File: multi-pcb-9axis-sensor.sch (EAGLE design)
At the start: 2 parts, among them X1 2.54B-ZR

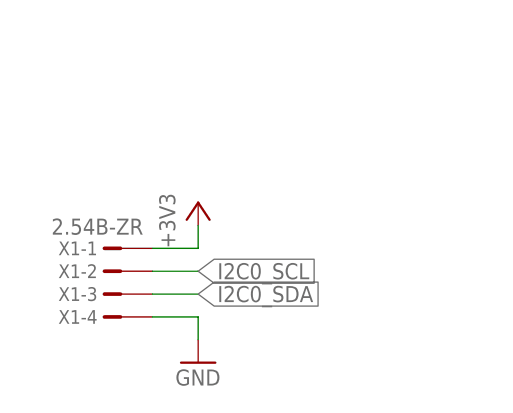
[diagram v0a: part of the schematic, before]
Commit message: Routed more multi-pcb boards
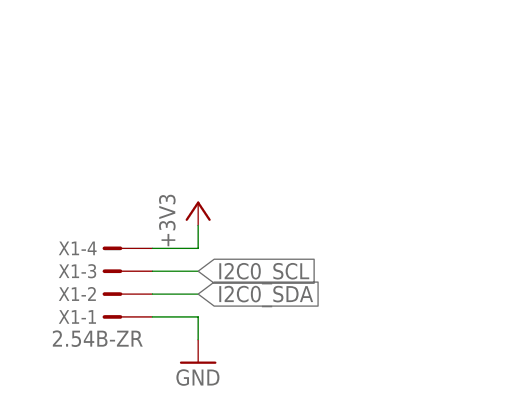
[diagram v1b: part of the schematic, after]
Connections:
- net +3V3: now also X1-4.1; no longer X1-1.1
- net GND: now also X1-1.1; no longer X1-4.1
- net I2C0_SCL: now also X1-3.1; no longer X1-2.1
- net I2C0_SDA: now also X1-2.1; no longer X1-3.1
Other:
- moved on the sheet: X1-1, X1-2, X1-3, X1-4
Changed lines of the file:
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@@
 <attribute name="VALUE" x="-109.22" y="-55.88" size="1.778" layer="96" rot="R90"/>
 </instance>
-<instance part="X1" gate="-1" x="-116.84" y="-55.88" smashed="yes" rot="MR0">
-<attribute name="NAME" x="-117.856" y="-56.642" size="1.524" layer="95" rot="MR0"/>
-<attribute name="VALUE" x="-112.776" y="-54.356" size="1.778" layer="96" rot="MR0"/>
+<instance part="X1" gate="-1" x="-116.84" y="-63.5" smashed="yes" rot="R180">
+<attribute name="NAME" x="-117.856" y="-62.738" size="1.524" layer="95" rot="R180"/>
+<attribute name="VALUE" x="-112.776" y="-65.024" size="1.778" layer="96" rot="R180"/>
 </instance>
-<instance part="X1" gate="-2" x="-116.84" y="-58.42" smashed="yes" rot="MR0">
-<attribute name="NAME" x="-117.856" y="-59.182" size="1.524" layer="95" rot="MR0"/>
+<instance part="X1" gate="-2" x="-116.84" y="-60.96" smashed="yes" rot="R180">
+<attribute name="NAME" x="-117.856" y="-60.198" size="1.524" layer="95" rot="R180"/>
 </instance>
-<instance part="X1" gate="-3" x="-116.84" y="-60.96" smashed="yes" rot="MR0">
-<attribute name="NAME" x="-117.856" y="-61.722" size="1.524" layer="95" rot="MR0"/>
+<instance part="X1" gate="-3" x="-116.84" y="-58.42" smashed="yes" rot="R180">
+<attribute name="NAME" x="-117.856" y="-57.658" size="1.524" layer="95" rot="R180"/>
 </instance>
-<instance part="X1" gate="-4" x="-116.84" y="-63.5" smashed="yes" rot="MR0">
-<attribute name="NAME" x="-117.856" y="-64.262" size="1.524" layer="95" rot="MR0"/>
+<instance part="X1" gate="-4" x="-116.84" y="-55.88" smashed="yes" rot="R180">
+<attribute name="NAME" x="-117.856" y="-55.118" size="1.524" layer="95" rot="R180"/>
 </instance>
 </instances>
@@
 <wire x1="-106.68" y1="-55.88" x2="-106.68" y2="-53.34" width="0.1524" layer="91"/>
 <pinref part="+3V1" gate="G$1" pin="+3V3"/>
-<pinref part="X1" gate="-1" pin="1"/>
-<wire x1="-106.68" y1="-55.88" x2="-111.76" y2="-55.88" width="0.1524" layer="91"/>
+<pinref part="X1" gate="-4" pin="1"/>
+<wire x1="-111.76" y1="-55.88" x2="-106.68" y2="-55.88" width="0.1524" layer="91"/>
 </segment>
 </net>
@@
 <wire x1="-106.68" y1="-63.5" x2="-106.68" y2="-66.04" width="0.1524" layer="91"/>
 <pinref part="GND15" gate="1" pin="GND"/>
-<pinref part="X1" gate="-4" pin="1"/>
+<pinref part="X1" gate="-1" pin="1"/>
 <wire x1="-106.68" y1="-63.5" x2="-111.76" y2="-63.5" width="0.1524" layer="91"/>
 </segment>
@@
 <segment>
 <label x="-106.68" y="-60.96" size="1.778" layer="95" xref="yes"/>
-<pinref part="X1" gate="-3" pin="1"/>
+<pinref part="X1" gate="-2" pin="1"/>
 <wire x1="-111.76" y1="-60.96" x2="-106.68" y2="-60.96" width="0.1524" layer="91"/>
 </segment>
@@
 <segment>
 <label x="-106.68" y="-58.42" size="1.778" layer="95" xref="yes"/>
-<pinref part="X1" gate="-2" pin="1"/>
+<pinref part="X1" gate="-3" pin="1"/>
 <wire x1="-106.68" y1="-58.42" x2="-111.76" y2="-58.42" width="0.1524" layer="91"/>
 </segment>

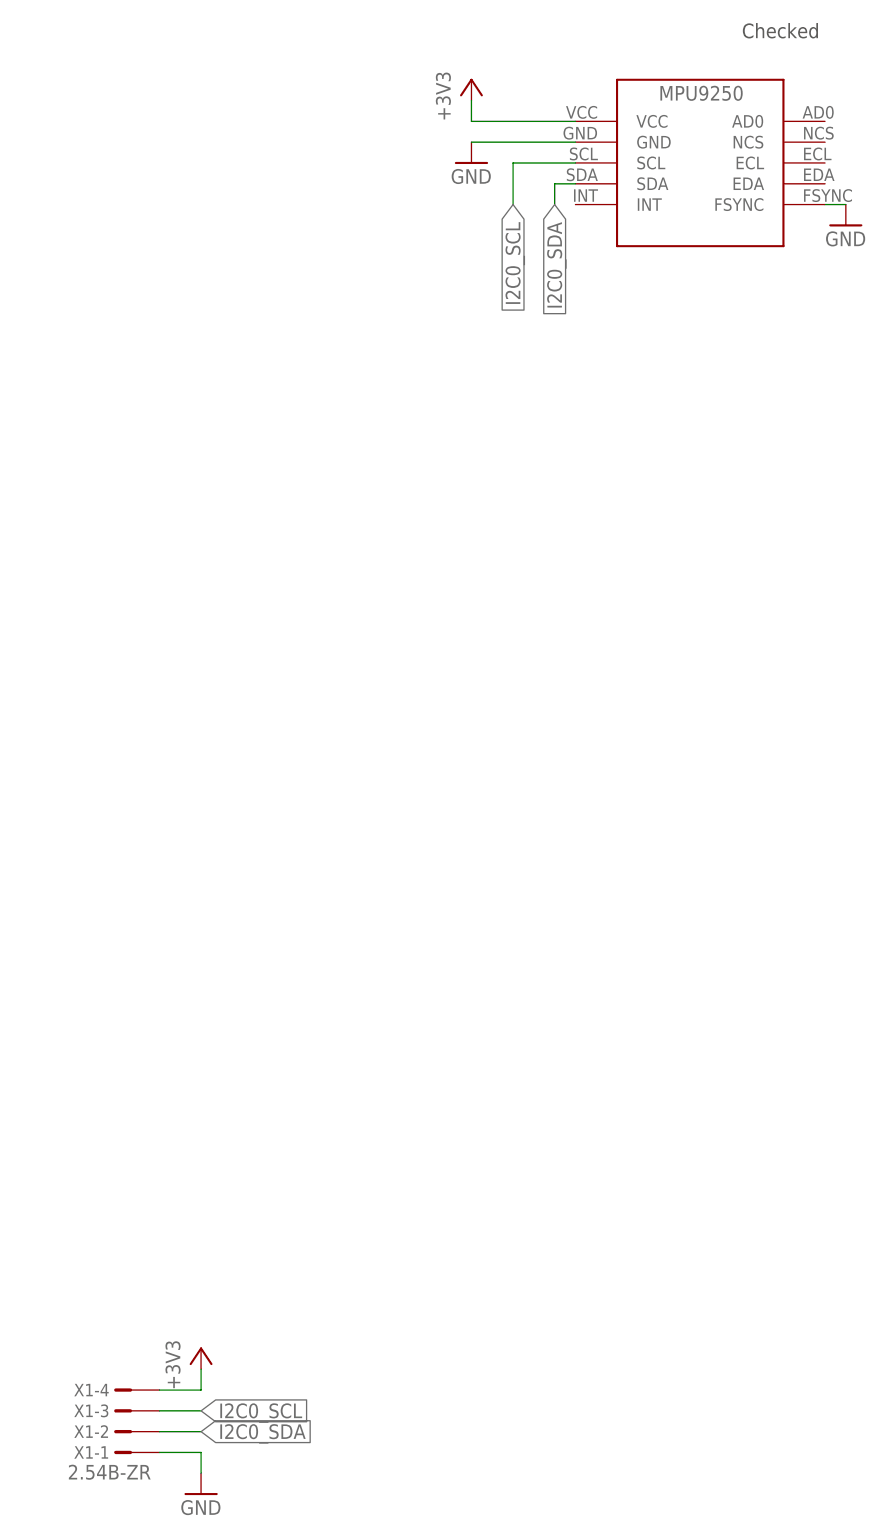
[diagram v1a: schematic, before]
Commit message: Made schematic more compact/clean
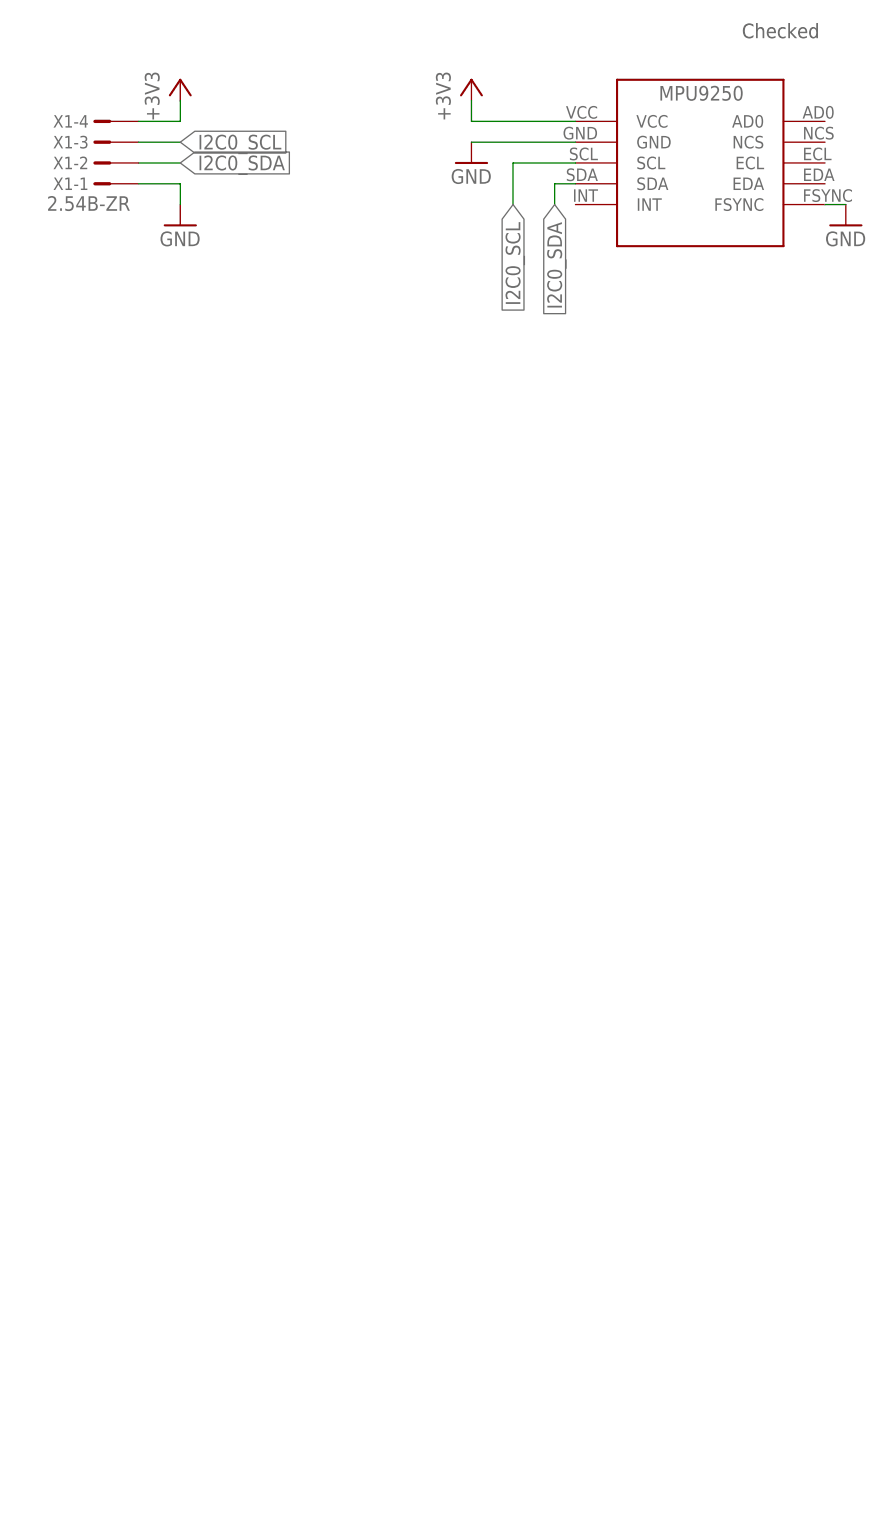
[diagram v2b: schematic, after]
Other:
- moved on the sheet: X1-1, X1-2, X1-3, X1-4
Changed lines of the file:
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@@
 <attribute name="VALUE" x="-30.48" y="83.82" size="1.778" layer="96"/>
 </instance>
-<instance part="GND15" gate="1" x="-106.68" y="-68.58" smashed="yes">
-<attribute name="VALUE" x="-109.22" y="-71.12" size="1.778" layer="96"/>
+<instance part="GND15" gate="1" x="-109.22" y="86.36" smashed="yes">
+<attribute name="VALUE" x="-111.76" y="83.82" size="1.778" layer="96"/>
 </instance>
 <instance part="+3V5" gate="G$1" x="-73.66" y="104.14" smashed="yes">
 <attribute name="VALUE" x="-76.2" y="99.06" size="1.778" layer="96" rot="R90"/>
 </instance>
-<instance part="+3V1" gate="G$1" x="-106.68" y="-50.8" smashed="yes">
-<attribute name="VALUE" x="-109.22" y="-55.88" size="1.778" layer="96" rot="R90"/>
+<instance part="+3V1" gate="G$1" x="-109.22" y="104.14" smashed="yes">
+<attribute name="VALUE" x="-111.76" y="99.06" size="1.778" layer="96" rot="R90"/>
 </instance>
-<instance part="X1" gate="-1" x="-116.84" y="-63.5" smashed="yes" rot="R180">
-<attribute name="NAME" x="-117.856" y="-62.738" size="1.524" layer="95" rot="R180"/>
-<attribute name="VALUE" x="-112.776" y="-65.024" size="1.778" layer="96" rot="R180"/>
+<instance part="X1" gate="-1" x="-119.38" y="91.44" smashed="yes" rot="R180">
+<attribute name="NAME" x="-120.396" y="92.202" size="1.524" layer="95" rot="R180"/>
+<attribute name="VALUE" x="-115.316" y="89.916" size="1.778" layer="96" rot="R180"/>
 </instance>
-<instance part="X1" gate="-2" x="-116.84" y="-60.96" smashed="yes" rot="R180">
-<attribute name="NAME" x="-117.856" y="-60.198" size="1.524" layer="95" rot="R180"/>
+<instance part="X1" gate="-2" x="-119.38" y="93.98" smashed="yes" rot="R180">
+<attribute name="NAME" x="-120.396" y="94.742" size="1.524" layer="95" rot="R180"/>
 </instance>
-<instance part="X1" gate="-3" x="-116.84" y="-58.42" smashed="yes" rot="R180">
-<attribute name="NAME" x="-117.856" y="-57.658" size="1.524" layer="95" rot="R180"/>
+<instance part="X1" gate="-3" x="-119.38" y="96.52" smashed="yes" rot="R180">
+<attribute name="NAME" x="-120.396" y="97.282" size="1.524" layer="95" rot="R180"/>
 </instance>
-<instance part="X1" gate="-4" x="-116.84" y="-55.88" smashed="yes" rot="R180">
-<attribute name="NAME" x="-117.856" y="-55.118" size="1.524" layer="95" rot="R180"/>
+<instance part="X1" gate="-4" x="-119.38" y="99.06" smashed="yes" rot="R180">
+<attribute name="NAME" x="-120.396" y="99.822" size="1.524" layer="95" rot="R180"/>
 </instance>
 </instances>
@@
 </segment>
 <segment>
-<wire x1="-106.68" y1="-55.88" x2="-106.68" y2="-53.34" width="0.1524" layer="91"/>
+<wire x1="-109.22" y1="99.06" x2="-109.22" y2="101.6" width="0.1524" layer="91"/>
 <pinref part="+3V1" gate="G$1" pin="+3V3"/>
 <pinref part="X1" gate="-4" pin="1"/>
-<wire x1="-111.76" y1="-55.88" x2="-106.68" y2="-55.88" width="0.1524" layer="91"/>
+<wire x1="-114.3" y1="99.06" x2="-109.22" y2="99.06" width="0.1524" layer="91"/>
 </segment>
 </net>
@@
 </segment>
 <segment>
-<wire x1="-106.68" y1="-63.5" x2="-106.68" y2="-66.04" width="0.1524" layer="91"/>
+<wire x1="-109.22" y1="91.44" x2="-109.22" y2="88.9" width="0.1524" layer="91"/>
 <pinref part="GND15" gate="1" pin="GND"/>
 <pinref part="X1" gate="-1" pin="1"/>
-<wire x1="-106.68" y1="-63.5" x2="-111.76" y2="-63.5" width="0.1524" layer="91"/>
+<wire x1="-109.22" y1="91.44" x2="-114.3" y2="91.44" width="0.1524" layer="91"/>
 </segment>
 </net>
@@
 </segment>
 <segment>
-<label x="-106.68" y="-60.96" size="1.778" layer="95" xref="yes"/>
+<label x="-109.22" y="93.98" size="1.778" layer="95" xref="yes"/>
 <pinref part="X1" gate="-2" pin="1"/>
-<wire x1="-111.76" y1="-60.96" x2="-106.68" y2="-60.96" width="0.1524" layer="91"/>
+<wire x1="-114.3" y1="93.98" x2="-109.22" y2="93.98" width="0.1524" layer="91"/>
 </segment>
 </net>
@@
 </segment>
 <segment>
-<label x="-106.68" y="-58.42" size="1.778" layer="95" xref="yes"/>
+<label x="-109.22" y="96.52" size="1.778" layer="95" xref="yes"/>
 <pinref part="X1" gate="-3" pin="1"/>
-<wire x1="-106.68" y1="-58.42" x2="-111.76" y2="-58.42" width="0.1524" layer="91"/>
+<wire x1="-109.22" y1="96.52" x2="-114.3" y2="96.52" width="0.1524" layer="91"/>
 </segment>
 </net>
